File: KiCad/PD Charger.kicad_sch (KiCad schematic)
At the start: 89 parts, among them J1 USB_C_Receptacle_USB2.0, J2 Conn_ARM_SWD_TagConnect_TC2030, J3 XT60_M, Q1 NMOS, Q2 NMOS, Q3 NMOS, Q4 NMOS, Q5 NTMFS002P03, Q6 NTMFS002P03, Q7 Q_Dual_NMOS_S1G1D2S2G2D1, Q8 Q_Dual_NMOS_S1G1D2S2G2D1, SW1 SW_MEC_5G, U1 FUSB302B01MPX, U2 LMR36006BRNXT, U3 LT8390xFE, U4 STM32G431C6Ux

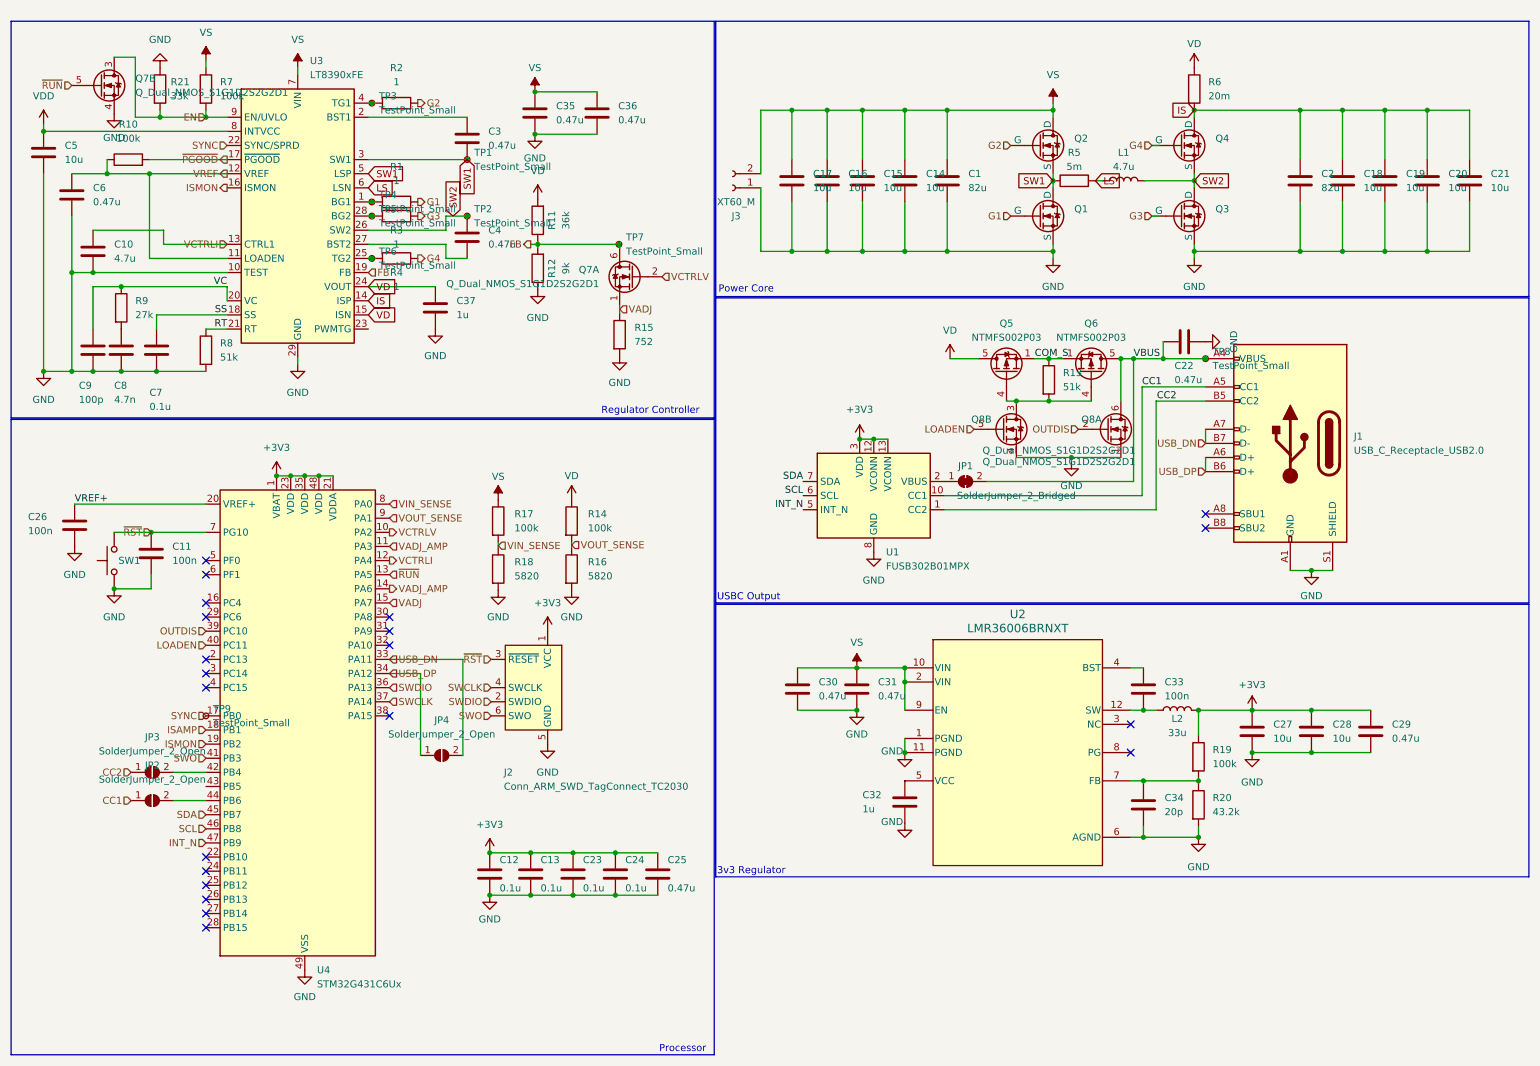
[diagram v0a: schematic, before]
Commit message: board update from tested issues
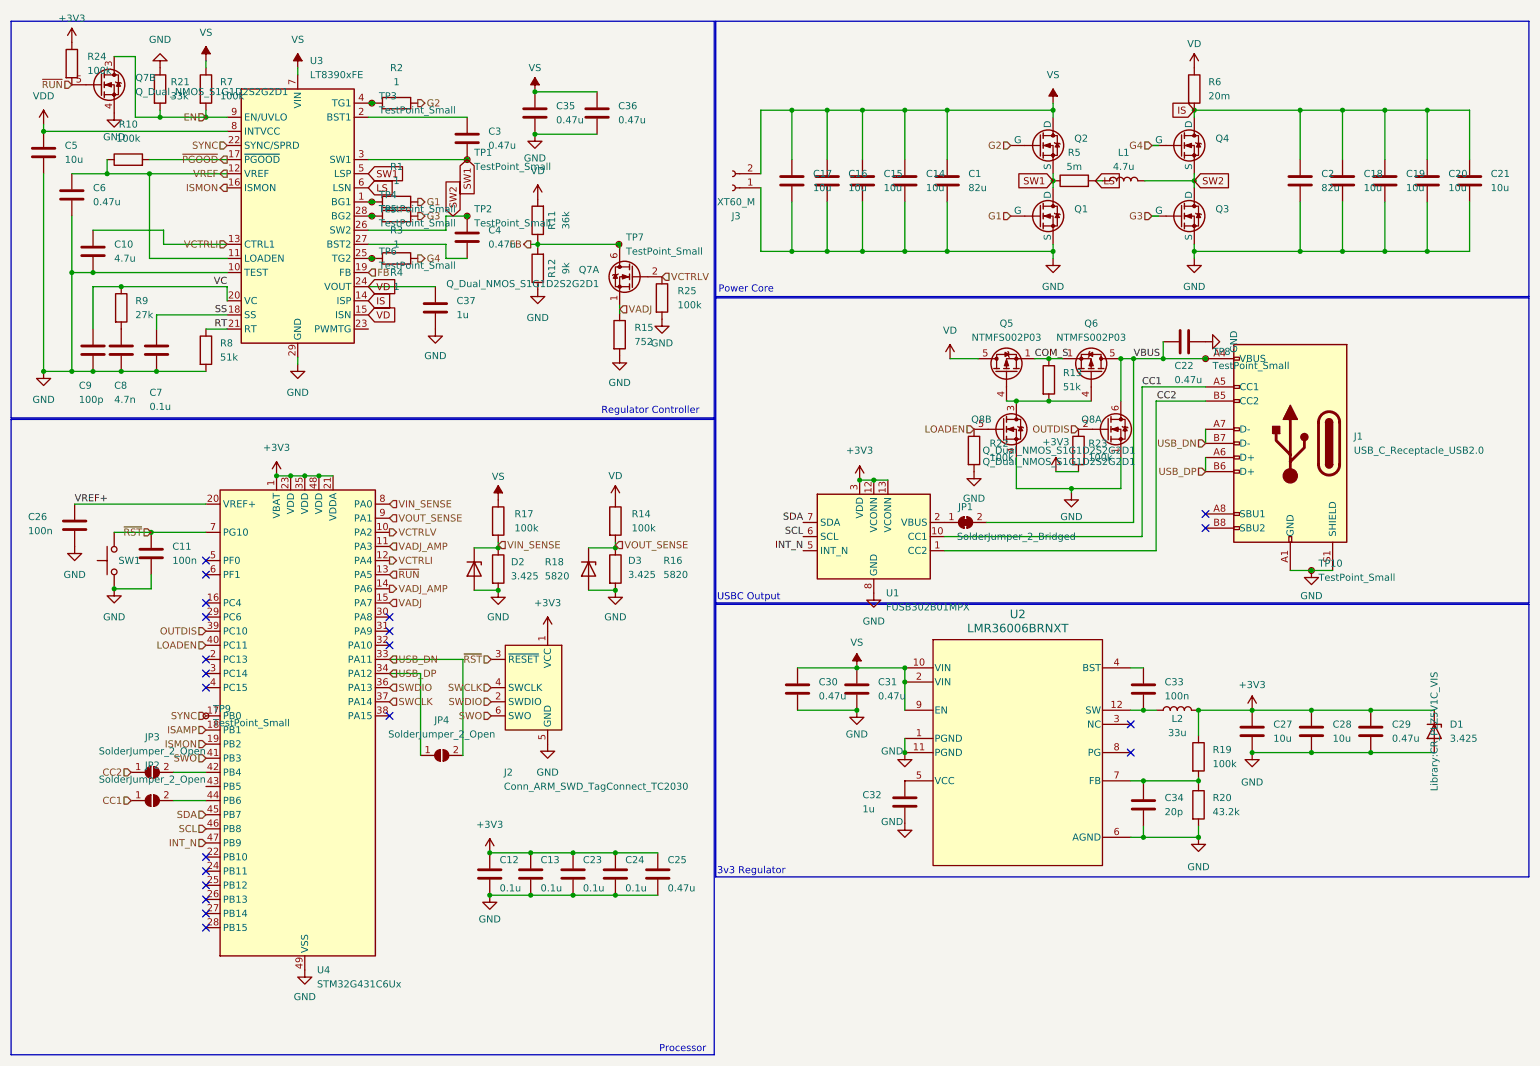
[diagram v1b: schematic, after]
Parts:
- added D1, D2, D3: 3.425, Library:CR_PLZ5V1C_VIS, symbol Device:D_Zener
- added R22, R23, R24, R25: 100k, Resistor_SMD:R_0603_1608Metric, symbol Device:R
- added TP10: TestPoint_Small, TestPoint:TestPoint_Pad_D1.0mm, symbol Connector:TestPoint_Small
- Q7, Q8: footprint Package_TO_SOT_SMD:SOT-23-6 -> Package_TO_SOT_SMD:SOT-363_SC-70-6
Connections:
- net +3V3: now also D1.1 (K), R23.2, R24.1
- net GND: now also D1.2 (A), D2.2 (A), D3.2 (A), R22.2, R25.2, TP10.1
- net LOADEN: now also R22.1
- net OUTDIS: now also R23.1
- net VCTRLV: now also R25.1
- net VIN_SENSE: now also D2.1 (K)
- net VOUT_SENSE: now also D3.1 (K)
- net ~{RUN}: now also R24.2
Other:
- moved on the sheet: JP1, R14, R16, U1

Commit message: board update
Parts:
- added R26, R27: 10k, Resistor_SMD:R_0603_1608Metric, symbol Device:R
- added SW2: SW_MEC_5G, Button_Switch_SMD:SW_SPST_B3U-1000P-B, symbol Switch:SW_Push
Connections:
- net +3V3: now also R26.1; no longer R24.1
- net GND: now also R24.1, R27.2
- net INT_N: now also U4.32 (PA10); no longer U4.47 (PB9)
- net SCL: now also U4.31 (PA9); no longer U4.46 (PB8)
- net SDA: now also U4.30 (PA8); no longer U4.45 (PB7)
- net VREF: no longer U3.11 (LOADEN)
- net ~{RST}: now also R26.2
- net REGEN: now reaches U4.2 (PC13)
- net REGEN: now also U3.11 (LOADEN)
- new net: R27.1, SW2.1
- new net BOOT0: SW2.2, U4.46 (PB8)
- no-connect marks 21 -> 19
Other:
- moved on the sheet: Q7B, R24

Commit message: better usbc & fusb302 routing
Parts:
- removed C16, C17: 10u, Capacitor_SMD:C_1206_3216Metric, symbol Device:C
- removed C22: 0.47u, Capacitor_SMD:C_0805_2012Metric, symbol Device:C
- added C12, C13: 10u, Capacitor_SMD:C_1206_3216Metric, symbol Device:C
- added C37, C38: 0.47u, Capacitor_SMD:C_0805_2012Metric, symbol Device:C
- added C39, C40, C43: 100n, Capacitor_SMD:C_0603_1608Metric, symbol Device:C
- added C41, C42: 330p, Capacitor_SMD:C_0603_1608Metric, symbol Device:C
- U4: value STM32G431C6Ux -> STM32G431CBUx
- renumbered C37 to C11, C18 to C16, C19 to C17, C20 to C18, C21 to C19, C12 to C20, C13 to C21, C23 to C22, C24 to C23, C25 to C24, C26 to C25, C11 to C26
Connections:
- net +3V3: now also C43.1
- net CC1: now also C41.1
- net CC2: now also C42.1
- net GND: now also C12.2, C13.2, C37.2, C38.2, C39.2, C40.2, C41.2, C42.2, C43.2
- net VBUS: now also C37.1, C38.1, C39.1, C40.1
- net VS: now also C12.1, C13.1

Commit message: multisheet design
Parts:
- removed C1, C2: 82u, Capacitor_SMD:CP_Elec_10x7.9, symbol Device:C
- removed C10: 4.7u, Capacitor_SMD:C_0603_1608Metric, symbol Device:C
- removed C11, C32: 1u, Capacitor_SMD:C_0603_1608Metric, symbol Device:C
- removed C12, C13, C14, C15, C16, C17, C18, C19, C27, C28, C5: 10u, Capacitor_SMD:C_1206_3216Metric, symbol Device:C
- removed C20, C21, C22, C23, C7: 0.1u, Capacitor_SMD:C_0603_1608Metric, symbol Device:C
- removed C24, C6: 0.47u, Capacitor_SMD:C_0603_1608Metric, symbol Device:C
- removed C25, C26, C33, C39, C40, C43: 100n, Capacitor_SMD:C_0603_1608Metric, symbol Device:C
- removed C29, C3, C30, C31, C35, C36, C37, C38, C4: 0.47u, Capacitor_SMD:C_0805_2012Metric, symbol Device:C
- removed C34: 20p, Capacitor_SMD:C_0603_1608Metric, symbol Device:C
- removed C41, C42: 330p, Capacitor_SMD:C_0603_1608Metric, symbol Device:C
- removed C8: 4.7n, Capacitor_SMD:C_0603_1608Metric, symbol Device:C
- removed C9: 100p, Capacitor_SMD:C_0603_1608Metric, symbol Device:C
- removed D1, D2, D3: 3.425, Library:CR_PLZ5V1C_VIS, symbol Device:D_Zener
- removed J2: Conn_ARM_SWD_TagConnect_TC2030, Connector:Tag-Connect_TC2030-IDC-NL_2x03_P1.27mm_Vertical, symbol Connector:Conn_ARM_SWD_TagConnect_TC2030
- removed JP1: SolderJumper_2_Bridged, Jumper:SolderJumper-2_P1.3mm_Bridged2Bar_RoundedPad1.0x1.5mm, symbol Jumper:SolderJumper_2_Bridged
- removed JP2, JP3, JP4: SolderJumper_2_Open, Jumper:SolderJumper-2_P1.3mm_Open_RoundedPad1.0x1.5mm, symbol Jumper:SolderJumper_2_Open
- removed L1: 4.7u, Inductor_SMD:L_Vishay_IHLP-6767, symbol Device:L
- removed L2: 33u, Inductor_SMD:L_Wuerth_MAPI-3015, symbol Device:L
- removed Q1, Q2, Q3, Q4: NMOS, Library:ECP2302, symbol Simulation_SPICE:NMOS
- removed Q5, Q6: NTMFS002P03, Package_DFN_QFN:AO_DFN-8-1EP_5.55x5.2mm_P1.27mm_EP4.12x4.6mm, symbol Transistor_FET:AON6411
- removed Q7, Q8: Q_Dual_NMOS_S1G1D2S2G2D1, Package_TO_SOT_SMD:SOT-363_SC-70-6, symbol Device:Q_Dual_NMOS_S1G1D2S2G2D1
- removed R1, R2, R3, R4: 1, Resistor_SMD:R_0603_1608Metric, symbol Device:R
- removed R10, R14, R17, R19, R22, R23, R24, R25, R7: 100k, Resistor_SMD:R_0603_1608Metric, symbol Device:R
- removed R11: 36k, Resistor_SMD:R_0603_1608Metric, symbol Device:R
- removed R12: 9k, Resistor_SMD:R_0603_1608Metric, symbol Device:R
- removed R13, R8: 51k, Resistor_SMD:R_0603_1608Metric, symbol Device:R
- removed R15: 752, Resistor_SMD:R_0603_1608Metric, symbol Device:R
- removed R16, R18: 5820, Resistor_SMD:R_0603_1608Metric, symbol Device:R
- removed R20: 43.2k, Resistor_SMD:R_0603_1608Metric, symbol Device:R
- removed R21: 33k, Resistor_SMD:R_0603_1608Metric, symbol Device:R
- removed R26, R27: 10k, Resistor_SMD:R_0603_1608Metric, symbol Device:R
- removed R5: 5m, Resistor_SMD:R_1206_3216Metric, symbol Device:R
- removed R6: 20m, Resistor_SMD:R_1206_3216Metric, symbol Device:R
- removed R9: 27k, Resistor_SMD:R_0603_1608Metric, symbol Device:R
- removed SW1, SW2: SW_MEC_5G, Button_Switch_SMD:SW_SPST_B3U-1000P-B, symbol Switch:SW_Push
- removed TP1, TP2, TP3, TP4, TP5, TP6, TP7, TP8, TP9: TestPoint_Small, TestPoint:TestPoint_Pad_D1.0mm, symbol Connector:TestPoint_Small
- removed U1: FUSB302B01MPX, Package_DFN_QFN:WQFN-14-1EP_2.5x2.5mm_P0.5mm_EP1.45x1.45mm, symbol Interface_USB:FUSB302B01MPX
- removed U2: LMR36006BRNXT, Library:RNX0012B, symbol 2024-04-12_02-42-06:LMR36006BRNXT
- removed U3: LT8390xFE, Package_SO:TSSOP-28-1EP_4.4x9.7mm_P0.65mm, symbol Driver_LED:LT8391xFE
- removed U4: STM32G431CBUx, Package_DFN_QFN:QFN-48-1EP_7x7mm_P0.5mm_EP5.6x5.6mm, symbol MCU_ST_STM32G4:STM32G431C6Ux
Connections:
- net VS: no longer J3.2 (Pin_2)
- net CC1 renamed CC
- net CC2 renamed VCONN
- new net VIN: J3.2 (Pin_2)
- no-connect marks 19 -> 2
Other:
- added sheet 3v3 Regulator (3v3_regulator.kicad_sch)
- added sheet DC-DC (dc-dc.kicad_sch)
- added sheet Input Protection (input.kicad_sch)
- added sheet MCU (mcu.kicad_sch)
- added sheet Output Switch (output.kicad_sch)
- added sheet USB-C (usb-c.kicad_sch)
- note removed: "3v3 Regulator"
- note removed: "Power Core"
- note removed: "Processor"
- note removed: "Regulator Controller"
- note removed: "USBC Output"
- moved on the sheet: J1, J3, TP10

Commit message: new layout
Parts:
- added U7: TPD4E05U06DQA, Package_SON:USON-10_2.5x1.0mm_P0.5mm, symbol Power_Protection:TPD4E05U06DQA
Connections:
- net CC: now also U7.5 (D2-), U7.6 (NC)
- net GND: now also U7.3 (GND), U7.8 (GND)
- net USB_DN: now also U7.4 (D2+), U7.7 (NC)
- net USB_DP: now also U7.2 (D1-), U7.9 (NC)
- net VCONN: now also U7.1 (D1+), U7.10 (NC)
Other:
- sheet Input Protection ports: added SOURCE_EN; removed ENABLE
- sheet MCU ports: added LOAD_EN, REG_ON, SGOOD, SOURCE_EN, ~{FAULT}, ~{PGOOD}; removed LOADEN

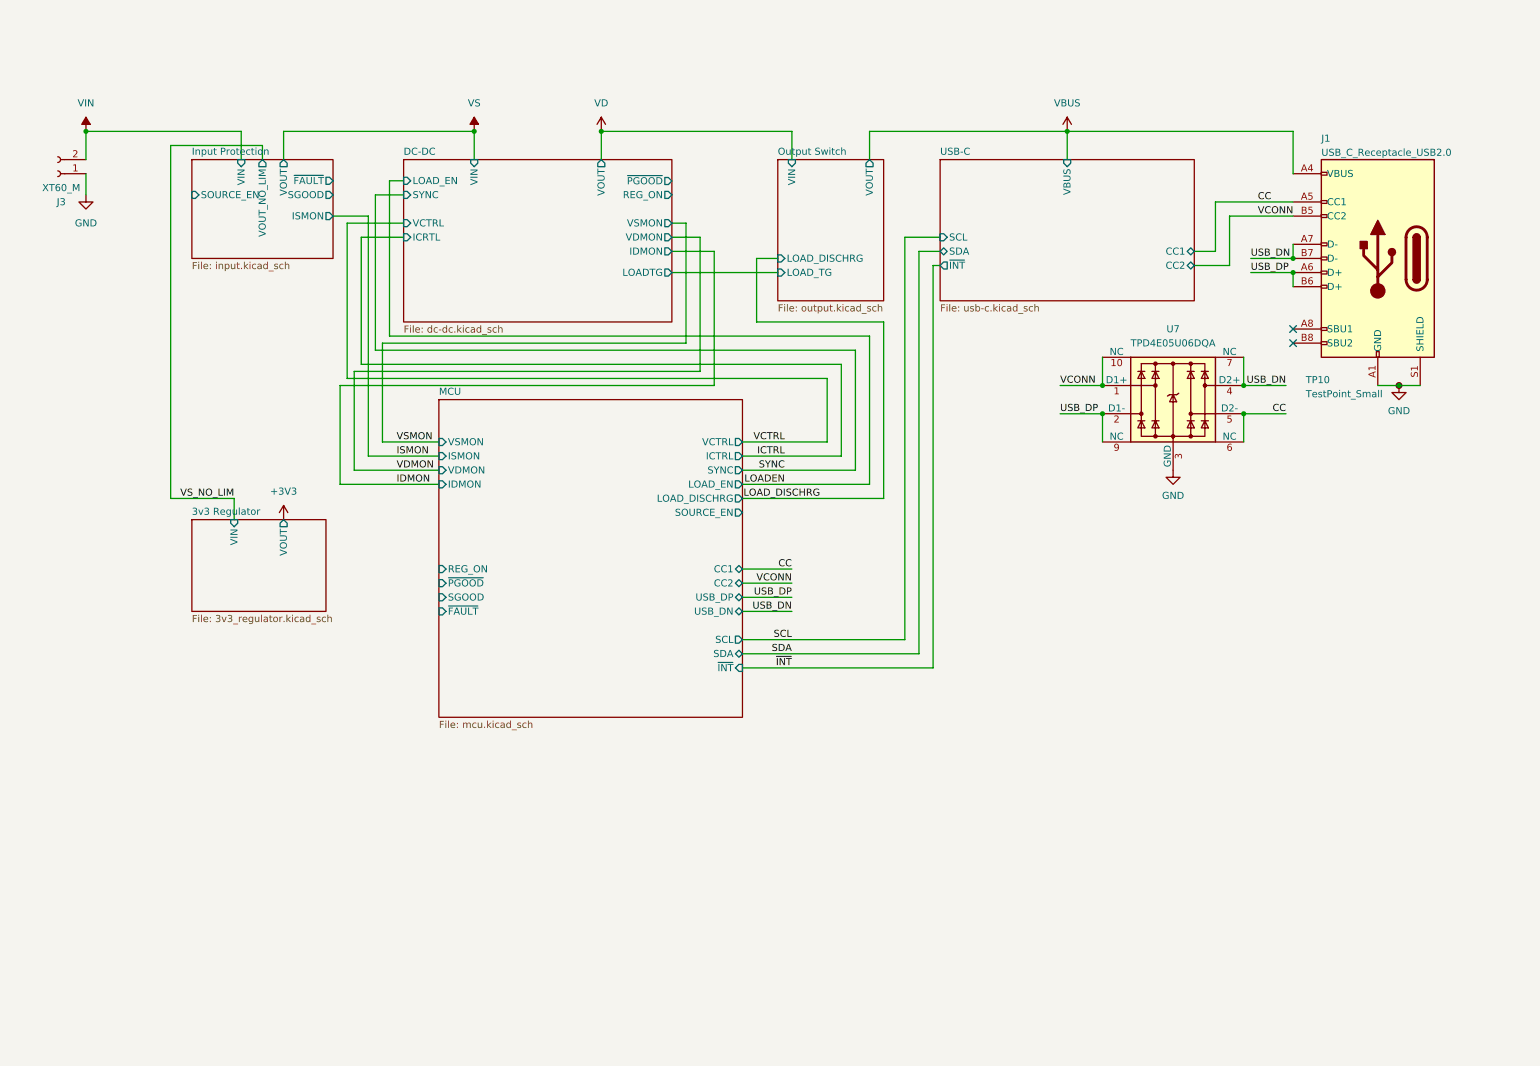
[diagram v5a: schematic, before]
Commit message: multi sheet redesign
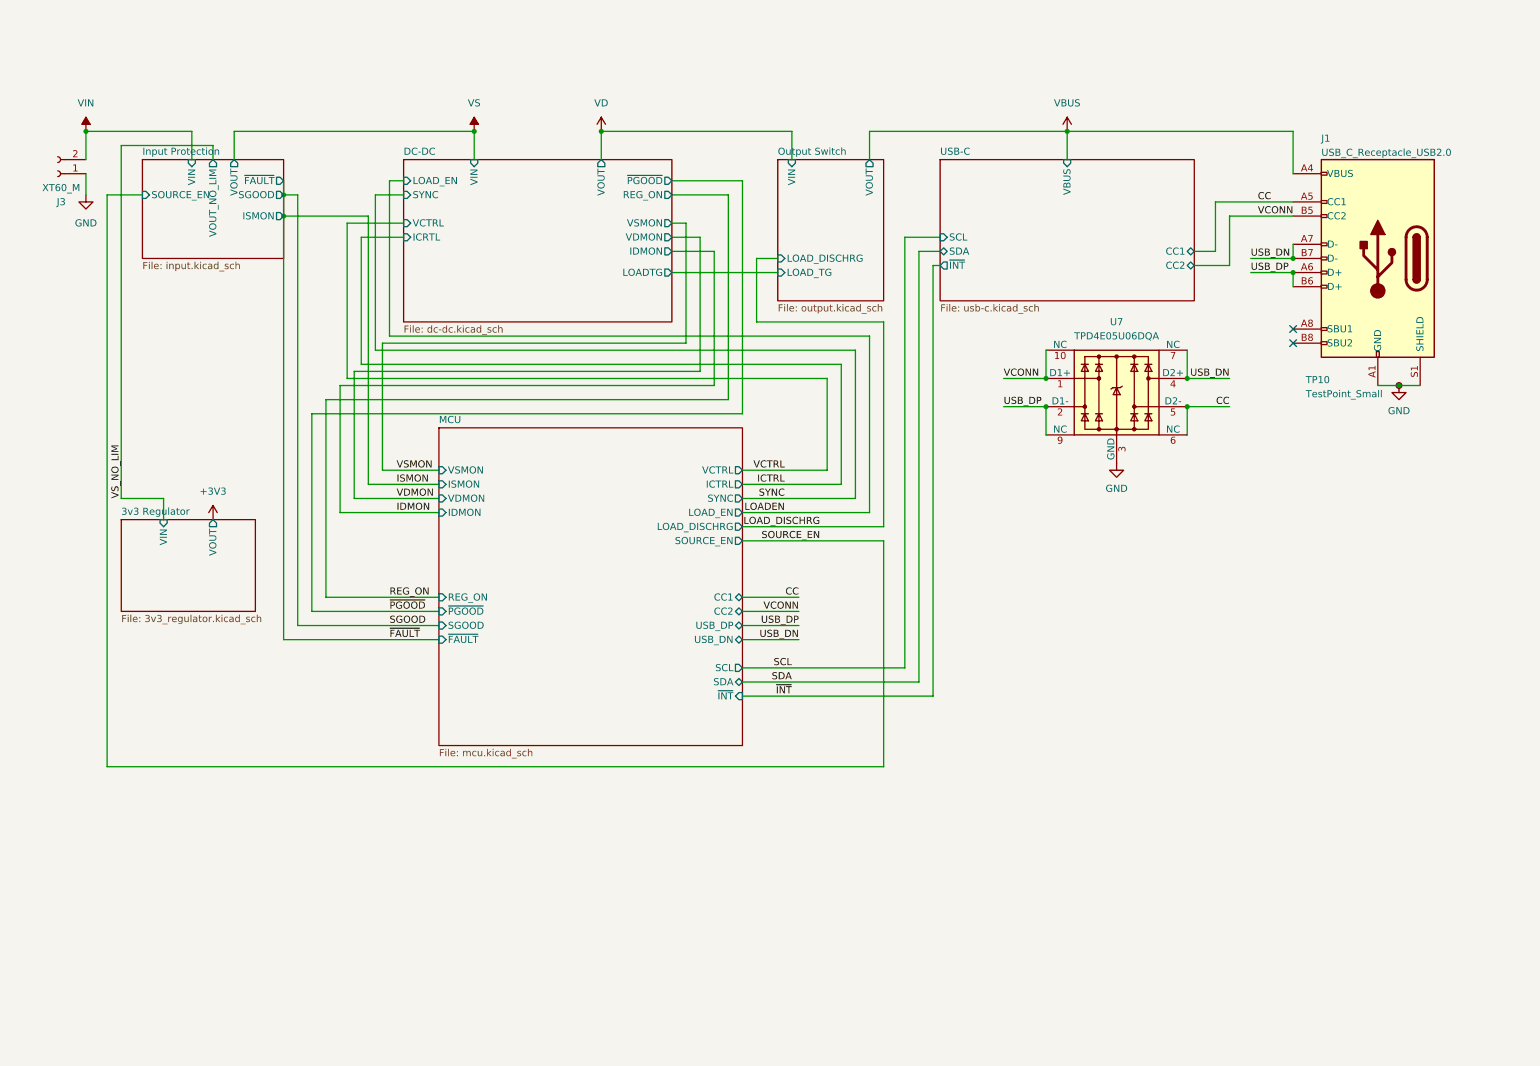
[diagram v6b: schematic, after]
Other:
- moved on the sheet: U7
